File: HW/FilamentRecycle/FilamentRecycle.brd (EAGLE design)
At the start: 100 x 80 mm, 22 parts, among them CON5 MOLEX-53261-0671, IC1 ATMEGA48A-AU, IC7 FT232RL, Q1 16MHz, Q2 BC847ALT1SMD, Q3 BC847ALT1SMD, X6 PN61729-S

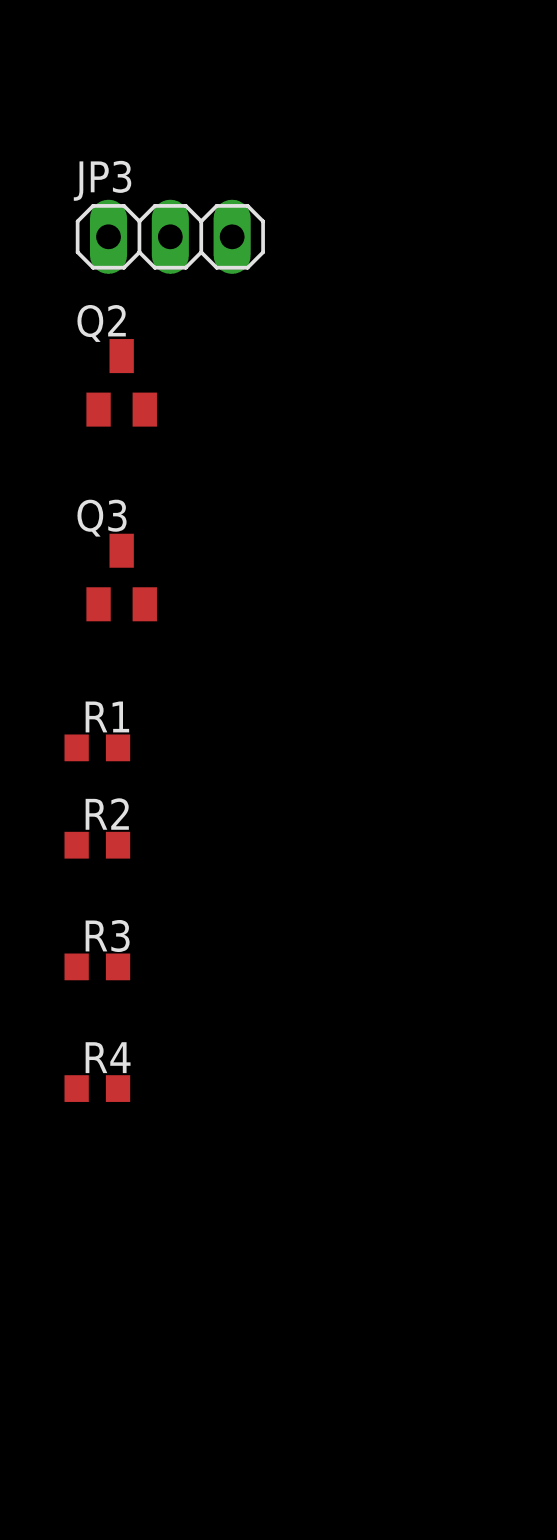
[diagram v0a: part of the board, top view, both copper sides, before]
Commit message: Reading the caliper via uart working
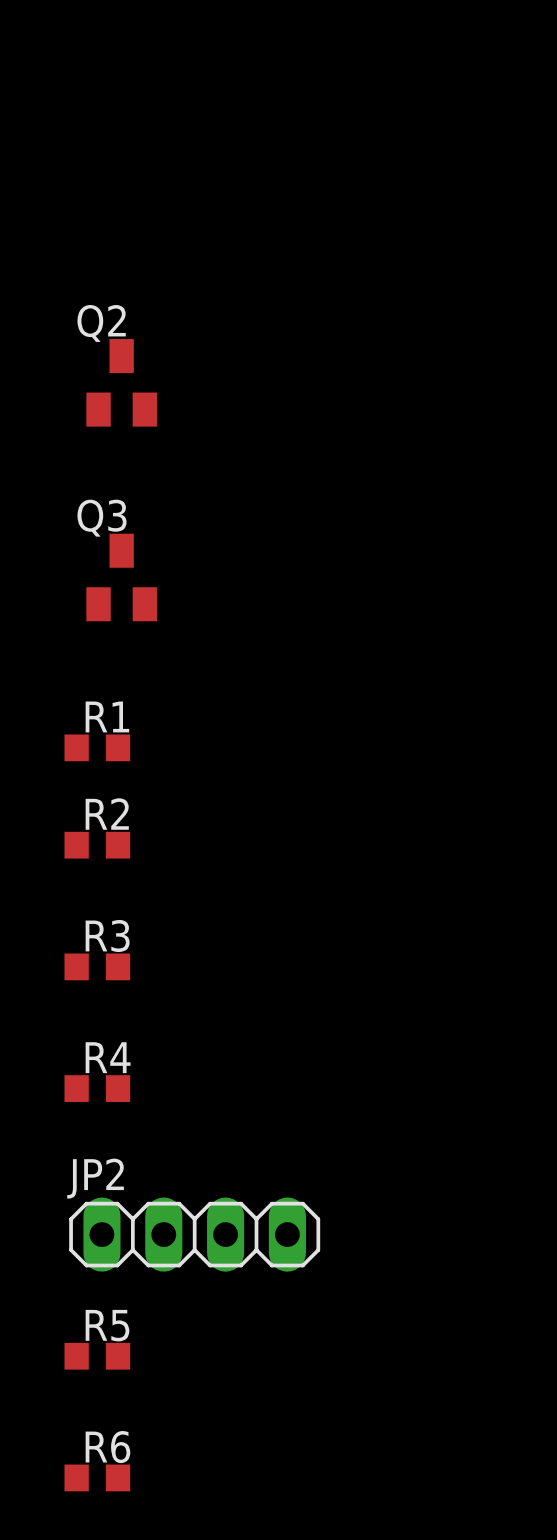
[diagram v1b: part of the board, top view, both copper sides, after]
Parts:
- removed JP3: (no value), pinhead:1X03
- added JP2: (no value), pinhead:1X04
- added R5: 390R, rcl:R0603
- added R6: 1k, rcl:R0603
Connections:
- removed net CALIPER_CLK_1V8: JP3.1, R1.1
- removed net CALIPER_DAT_1V8: JP3.3, R2.1
- removed net X_DIR: IC1.9
- removed net X_STEP: IC1.32
- removed net Y_DIR: IC1.10
- removed net Y_STEP: IC1.1
- removed net Z_DIR: IC1.11
- removed net Z_STEP: IC1.2
- new net CALIPER_CLK_1V5: JP2.2, R1.1
- new net CALIPER_DAT_1V5: JP2.3, R2.1
- new net CALIPER_SUPPLY: JP2.1, R5.2, R6.1
- net +5V: now also R6.2
- net CALIPER_CLK_3V3: now also IC1.32; no longer IC1.17
- net CALIPER_DAT_3V3: now also IC1.2; no longer IC1.16
- net GND: now also JP2.4, R5.1; no longer JP3.2
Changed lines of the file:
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@@
 <attribute name="OC_FARNELL" value="unknown" x="-9" y="-68" size="1.778" layer="27" display="off"/>
 </element>
-<element name="JP3" library="pinhead" package="1X03" value="" x="5" y="-83"/>
 <element name="Q2" library="transistor-npn" package="SOT23" value="BC847ALT1SMD" x="3" y="-89"/>
 <element name="Q3" library="transistor-npn" package="SOT23" value="BC847ALT1SMD" x="3" y="-97"/>
@@
 <element name="R3" library="rcl" package="R0603" value="10k" x="2" y="-113"/>
 <element name="R4" library="rcl" package="R0603" value="10k" x="2" y="-118"/>
+<element name="JP2" library="pinhead" package="1X04" value="" x="6" y="-124"/>
+<element name="R5" library="rcl" package="R0603" value="390R" x="2" y="-129"/>
+<element name="R6" library="rcl" package="R0603" value="1k" x="2" y="-134"/>
 </elements>
 <signals>
@@
 <contactref element="C8" pad="1"/>
 <contactref element="C9" pad="1"/>
-<contactref element="JP3" pad="2"/>
 <contactref element="Q2" pad="2"/>
 <contactref element="Q3" pad="2"/>
+<contactref element="JP2" pad="4"/>
+<contactref element="R5" pad="1"/>
+<wire x1="9.81" y1="-124" x2="1.15" y2="-129" width="0" layer="19" extent="1-1"/>
+<wire x1="3.95" y1="-98.1" x2="9.81" y2="-124" width="0" layer="19" extent="1-1"/>
 <wire x1="3.95" y1="-90.1" x2="3.95" y2="-98.1" width="0" layer="19" extent="1-1"/>
-<wire x1="5" y1="-83" x2="3.95" y2="-90.1" width="0" layer="19" extent="1-1"/>
-<wire x1="6.15" y1="-71" x2="5" y2="-83" width="0" layer="19" extent="1-1"/>
+<wire x1="6.15" y1="-71" x2="3.95" y2="-90.1" width="0" layer="19" extent="1-1"/>
 <wire x1="1.15" y1="-71" x2="6.15" y2="-71" width="0" layer="19" extent="1-1"/>
 <wire x1="1.25" y1="-64.35" x2="1.15" y2="-71" width="0" layer="19" extent="1-1"/>
@@
 <contactref element="R3" pad="2"/>
 <contactref element="R4" pad="2"/>
+<contactref element="R6" pad="2"/>
+<wire x1="2.85" y1="-118" x2="2.85" y2="-134" width="0" layer="19" extent="1-1"/>
 <wire x1="2.85" y1="-113" x2="2.85" y2="-118" width="0" layer="19" extent="1-1"/>
 <wire x1="2.85" y1="-71" x2="2.85" y2="-113" width="0" layer="19" extent="1-1"/>
@@
 <contactref element="CON5" pad="2"/>
 </signal>
-<signal name="Z_DIR">
-<contactref element="IC1" pad="11"/>
-</signal>
-<signal name="Y_DIR">
-<contactref element="IC1" pad="10"/>
-</signal>
-<signal name="X_DIR">
-<contactref element="IC1" pad="9"/>
-</signal>
-<signal name="Z_STEP">
-<contactref element="IC1" pad="2"/>
-</signal>
-<signal name="Y_STEP">
-<contactref element="IC1" pad="1"/>
-</signal>
-<signal name="X_STEP">
-<contactref element="IC1" pad="32"/>
-</signal>
 <signal name="SCK">
 <contactref element="CON5" pad="4"/>
@@
 </signal>
 <signal name="CALIPER_CLK_3V3">
-<contactref element="IC1" pad="17"/>
 <contactref element="Q2" pad="3"/>
 <contactref element="R3" pad="1"/>
+<contactref element="IC1" pad="32"/>
 <wire x1="3" y1="-87.9" x2="1.15" y2="-113" width="0" layer="19" extent="1-1"/>
-<wire x1="10.2926" y1="-9.8" x2="3" y2="-87.9" width="0" layer="19" extent="1-1"/>
+<wire x1="3.2" y1="-2.7074" x2="3" y2="-87.9" width="0" layer="19" extent="1-1"/>
 </signal>
 <signal name="CALIPER_DAT_3V3">
-<contactref element="IC1" pad="16"/>
 <contactref element="Q3" pad="3"/>
 <contactref element="R4" pad="1"/>
+<contactref element="IC1" pad="2"/>
 <wire x1="3" y1="-95.9" x2="1.15" y2="-118" width="0" layer="19" extent="1-1"/>
-<wire x1="8.8" y1="-11.2926" x2="3" y2="-95.9" width="0" layer="19" extent="1-1"/>
-</signal>
-<signal name="CALIPER_DAT_1V8">
-<contactref element="JP3" pad="3"/>
+<wire x1="1.7074" y1="-5" x2="3" y2="-95.9" width="0" layer="19" extent="1-1"/>
+</signal>
+<signal name="CALIPER_DAT_1V5">
 <contactref element="R2" pad="1"/>
-<wire x1="7.54" y1="-83" x2="1.15" y2="-108" width="0" layer="19" extent="1-1"/>
-</signal>
-<signal name="CALIPER_CLK_1V8">
-<contactref element="JP3" pad="1"/>
+<contactref element="JP2" pad="3"/>
+<wire x1="1.15" y1="-108" x2="7.27" y2="-124" width="0" layer="19" extent="1-1"/>
+</signal>
+<signal name="CALIPER_CLK_1V5">
 <contactref element="R1" pad="1"/>
-<wire x1="2.46" y1="-83" x2="1.15" y2="-104" width="0" layer="19" extent="1-1"/>
+<contactref element="JP2" pad="2"/>
+<wire x1="1.15" y1="-104" x2="4.73" y2="-124" width="0" layer="19" extent="1-1"/>
 </signal>
 <signal name="N$7">
@@
 <wire x1="2.05" y1="-98.1" x2="2.85" y2="-108" width="0" layer="19" extent="1-1"/>
 </signal>
+<signal name="CALIPER_SUPPLY">
+<contactref element="R5" pad="2"/>
+<contactref element="R6" pad="1"/>
+<contactref element="JP2" pad="1"/>
+<wire x1="2.85" y1="-129" x2="1.15" y2="-134" width="0" layer="19" extent="1-1"/>
+<wire x1="2.19" y1="-124" x2="2.85" y2="-129" width="0" layer="19" extent="1-1"/>
+</signal>
 </signals>

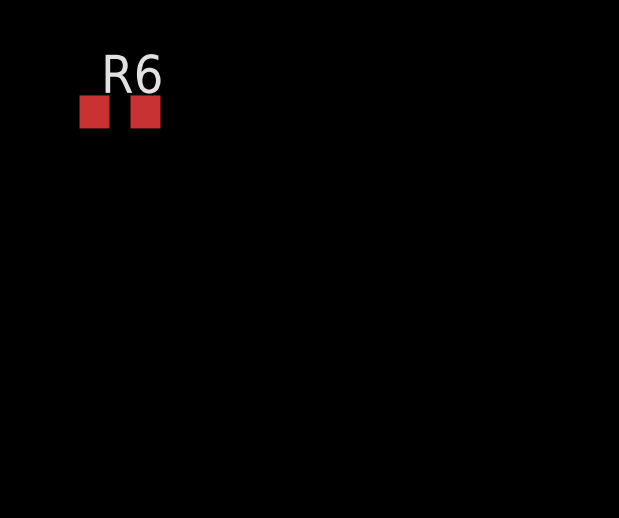
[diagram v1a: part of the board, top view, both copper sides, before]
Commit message: first version of NTC handling
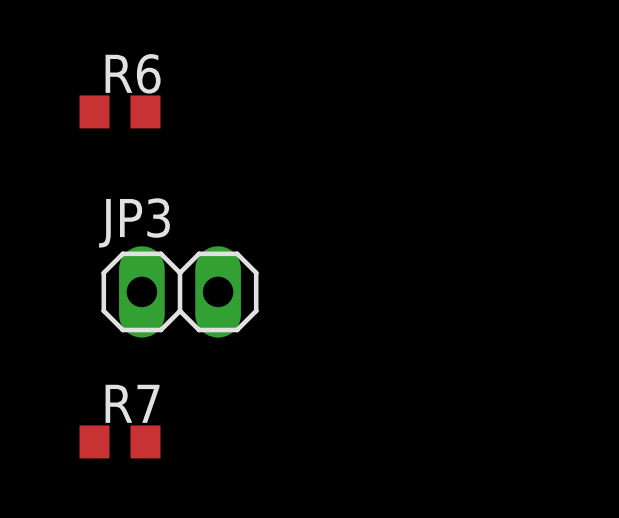
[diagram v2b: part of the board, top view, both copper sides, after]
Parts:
- added JP3: (no value), pinhead:1X02
- added R7: 10k, rcl:R0603
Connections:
- new net NTC_SIG: IC1.23, JP3.1, R7.2
- net +5V: now also R7.1
- net CALIPER_CLK_3V3: now also IC1.12; no longer IC1.32
- net CALIPER_DAT_3V3: now also IC1.13; no longer IC1.2
- net GND: now also JP3.2
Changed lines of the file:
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@@
 <element name="R5" library="rcl" package="R0603" value="390R" x="2" y="-129"/>
 <element name="R6" library="rcl" package="R0603" value="1k" x="2" y="-134"/>
+<element name="JP3" library="pinhead" package="1X02" value="" x="4" y="-140"/>
+<element name="R7" library="rcl" package="R0603" value="10k" x="2" y="-145"/>
 </elements>
 <signals>
@@
 <contactref element="JP2" pad="4"/>
 <contactref element="R5" pad="1"/>
+<contactref element="JP3" pad="2"/>
+<wire x1="1.15" y1="-129" x2="5.27" y2="-140" width="0" layer="19" extent="1-1"/>
 <wire x1="9.81" y1="-124" x2="1.15" y2="-129" width="0" layer="19" extent="1-1"/>
 <wire x1="3.95" y1="-98.1" x2="9.81" y2="-124" width="0" layer="19" extent="1-1"/>
@@
 <contactref element="R4" pad="2"/>
 <contactref element="R6" pad="2"/>
+<contactref element="R7" pad="1"/>
+<wire x1="2.85" y1="-134" x2="1.15" y2="-145" width="0" layer="19" extent="1-1"/>
 <wire x1="2.85" y1="-118" x2="2.85" y2="-134" width="0" layer="19" extent="1-1"/>
 <wire x1="2.85" y1="-113" x2="2.85" y2="-118" width="0" layer="19" extent="1-1"/>
@@
 <contactref element="Q2" pad="3"/>
 <contactref element="R3" pad="1"/>
-<contactref element="IC1" pad="32"/>
+<contactref element="IC1" pad="12"/>
 <wire x1="3" y1="-87.9" x2="1.15" y2="-113" width="0" layer="19" extent="1-1"/>
-<wire x1="3.2" y1="-2.7074" x2="3" y2="-87.9" width="0" layer="19" extent="1-1"/>
+<wire x1="5.6" y1="-11.2926" x2="3" y2="-87.9" width="0" layer="19" extent="1-1"/>
 </signal>
 <signal name="CALIPER_DAT_3V3">
 <contactref element="Q3" pad="3"/>
 <contactref element="R4" pad="1"/>
-<contactref element="IC1" pad="2"/>
+<contactref element="IC1" pad="13"/>
 <wire x1="3" y1="-95.9" x2="1.15" y2="-118" width="0" layer="19" extent="1-1"/>
-<wire x1="1.7074" y1="-5" x2="3" y2="-95.9" width="0" layer="19" extent="1-1"/>
+<wire x1="6.4" y1="-11.2926" x2="3" y2="-95.9" width="0" layer="19" extent="1-1"/>
 </signal>
 <signal name="CALIPER_DAT_1V5">
@@
 <wire x1="2.19" y1="-124" x2="2.85" y2="-129" width="0" layer="19" extent="1-1"/>
 </signal>
+<signal name="NTC_SIG">
+<contactref element="IC1" pad="23"/>
+<contactref element="JP3" pad="1"/>
+<contactref element="R7" pad="2"/>
+<wire x1="2.73" y1="-140" x2="2.85" y2="-145" width="0" layer="19" extent="1-1"/>
+<wire x1="10.2926" y1="-5" x2="2.73" y2="-140" width="0" layer="19" extent="1-1"/>
+</signal>
 </signals>

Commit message: Temperatur reading working with NTC3950 thermistor
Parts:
- R7: value 10k -> 4k7
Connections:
- removed net SPINDLE_ENABLE: CON5.2
- new net MISO: CON5.2, IC1.16
- net MOSI: now also IC1.15
- net SCK: now also IC1.17
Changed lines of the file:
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@@
 <element name="R6" library="rcl" package="R0603" value="1k" x="2" y="-134"/>
 <element name="JP3" library="pinhead" package="1X02" value="" x="4" y="-140"/>
-<element name="R7" library="rcl" package="R0603" value="10k" x="2" y="-145"/>
+<element name="R7" library="rcl" package="R0603" value="4k7" x="2" y="-145"/>
 </elements>
 <signals>
@@
 <wire x1="1.7074" y1="-9" x2="12.826" y2="-17" width="0" layer="19" extent="1-1"/>
 </signal>
-<signal name="SPINDLE_ENABLE">
+<signal name="MISO">
 <contactref element="CON5" pad="2"/>
+<contactref element="IC1" pad="16"/>
+<wire x1="8.8" y1="-11.2926" x2="5.125" y2="-61.45" width="0" layer="19" extent="1-1"/>
 </signal>
 <signal name="SCK">
 <contactref element="CON5" pad="4"/>
+<contactref element="IC1" pad="17"/>
+<wire x1="10.2926" y1="-9.8" x2="7.625" y2="-61.45" width="0" layer="19" extent="1-1"/>
 </signal>
 <signal name="MOSI">
 <contactref element="CON5" pad="1"/>
+<contactref element="IC1" pad="15"/>
+<wire x1="8" y1="-11.2926" x2="3.875" y2="-61.45" width="0" layer="19" extent="1-1"/>
 </signal>
 <signal name="USB_D-">

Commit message: Schematic and board work
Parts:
- added IC2: 74HC595D, 74xx-eu:SO16
- added JP4: (no value), pinhead:1X02
- added JP5, JP6: (no value), pinhead:2X03
- added JP7, JP8: (no value), pinhead:1X04
- added R10, R13, R15, R17, R19, R21, R23, R8: 50k, rcl:R0603
- added R12, R14, R16, R18, R20, R22, R24, R25, R28, R9: 100k, rcl:R0603
- added R26, R27: 10k, rcl:R0603
- added S1: (no value), switch-omron:B3F-10XX
- added U$14, U$7: A4988BREAKOUT, RepRapjr:A4988BREAKOUT
- moved R7 221.9 mm to (18.9, 76.2), flipped to the bottom, turned to 90 degrees
- moved JP3 218.0 mm to (23.0, 77.1)
- moved R6 210.0 mm to (14.5, 75.6), flipped to the bottom, turned to 180 degrees
- moved R5 207.6 mm to (14.5, 78.2), flipped to the bottom
- moved JP2 201.0 mm to (7.25, 77.0), turned to 180 degrees
- moved R4 185.4 mm to (3.00, 67.4), flipped to the bottom
- moved R2 181.8 mm to (6.00, 73.8), flipped to the bottom, turned to 270 degrees
- moved R3 179.7 mm to (7.88, 66.6), flipped to the bottom
- moved R1 177.9 mm to (8.50, 73.8), flipped to the bottom, turned to 270 degrees
- moved Q3 167.3 mm to (5.00, 70.2), flipped to the bottom, turned to 270 degrees
- moved Q2 158.9 mm to (8.75, 69.8), flipped to the bottom, turned to 180 degrees
- moved CON5 119.3 mm to (3.00, 55.2), flipped to the bottom, turned to 90 degrees
- moved JP1 92.1 mm to (8.50, 25.2)
- moved C11 87.8 mm to (15.0, 16.8), flipped to the bottom, turned to 270 degrees
- moved C9 87.2 mm to (26.2, 14.0), flipped to the bottom
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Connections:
- new net !MOT_SPINDLE_EN: R26.2, U$7.EN
- new net !MOT_WINDING_EN: R27.2, U$14.EN
- new net +12V: U$14.VMOT, U$7.VMOT
- new net DAC_CLK: IC1.27, IC2.11
- new net DAC_MISO: IC1.25, IC2.13
- new net DAC_MOSI: IC1.24, IC2.14
- new net DAC_SS: IC1.26, IC2.12
- new net MOT_SPINDLE_DIR: U$7.DIR
- new net MOT_SPINDLE_STEP: U$7.STEP
- new net MOT_WINDING_DIR: U$14.DIR
- new net MOT_WINDING_STEP: U$14.STEP
- new net N$10: R15.2, R17.1, R18.2
- new net N$11: R13.2, R15.1, R16.2
- new net N$12: R10.2, R13.1, R14.2
- new net N$13: R10.1, R12.2, R8.2
- new net N$14: R23.1, R8.1, R9.2
- new net N$15: IC2.15, R9.1
- new net N$16: IC2.1, R12.1
- new net N$17: IC2.2, R14.1
- new net N$18: IC2.3, R16.1
- new net N$19: IC2.4, R18.1
- new net N$20: IC2.5, R20.1
- new net N$21: IC2.6, R22.1
- new net N$22: IC2.7, R24.1
- new net N$23: JP5.5, U$7.MS3
- new net N$24: U$7.RST, U$7.SLP
- new net N$25: JP5.1, R25.1, U$7.MS1
- new net N$26: JP5.3, U$7.MS2
- new net N$27: JP7.1, U$7.2B
- new net N$28: JP7.2, U$7.2A
- new net N$29: JP7.3, U$7.1A
- new net N$3: JP4.1, R21.2, R24.2
- new net N$30: JP7.4, U$7.1B
- new net N$31: U$7.GND
- new net N$32: JP6.5, U$14.MS3
- new net N$33: JP6.1, R28.1, U$14.MS1
- new net N$34: JP6.3, U$14.MS2
- new net N$35: JP8.1, U$14.2B
- new net N$36: JP8.2, U$14.2A
- new net N$37: JP8.3, U$14.1A
- new net N$38: JP8.4, U$14.1B
- new net N$39: U$14.RST, U$14.SLP
- new net N$4: R19.2, R21.1, R22.2
- new net N$40: U$14.GND
- new net N$6: R17.2, R19.1, R20.2
- new net SS: IC1.14
- new net VCC: IC2.16
- net !RESET: now also S1.1, S1.2
- net +5V: now also IC2.10, JP5.2, JP5.4, JP5.6, JP6.2, JP6.4, JP6.6, U$14.VDD, U$7.VDD
- net CALIPER_CLK_3V3: now also IC1.22; no longer IC1.12
- net CALIPER_DAT_3V3: now also IC1.19; no longer IC1.13
- net GND: now also IC2.8, JP4.2, R23.2, R25.2, R26.1, R27.1, R28.2, S1.3, U$14.GND@0, U$7.GND@0
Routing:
- net N$15: track 0.00 -> 21.6 mm
- net N$14: track 0.00 -> 19.4 mm
- net N$13: track 0.00 -> 18.5 mm
- net N$2: track 0.00 -> 14.9 mm
- net N$1: track 0.00 -> 14.9 mm
- net +5V: track 0.00 -> 10.6 mm
- net SCK: track 0.00 -> 8.74 mm
- net MOSI: track 0.00 -> 7.17 mm
- net MISO: track 0.00 -> 6.98 mm
- net N$22: track 0.00 -> 5.52 mm
- net N$3: track 0.00 -> 5.32 mm
- net CALIPER_SUPPLY: track 0.00 -> 5.27 mm
- net N$16: track 0.00 -> 4.95 mm
- net N$17: track 0.00 -> 4.89 mm
- net N$10: track 0.00 -> 4.83 mm
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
